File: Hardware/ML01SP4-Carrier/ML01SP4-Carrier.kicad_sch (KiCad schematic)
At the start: 3 parts, among them J1 NRF24L01P-ML01SP4, J2 Conn_01x05, J3 Conn_01x03

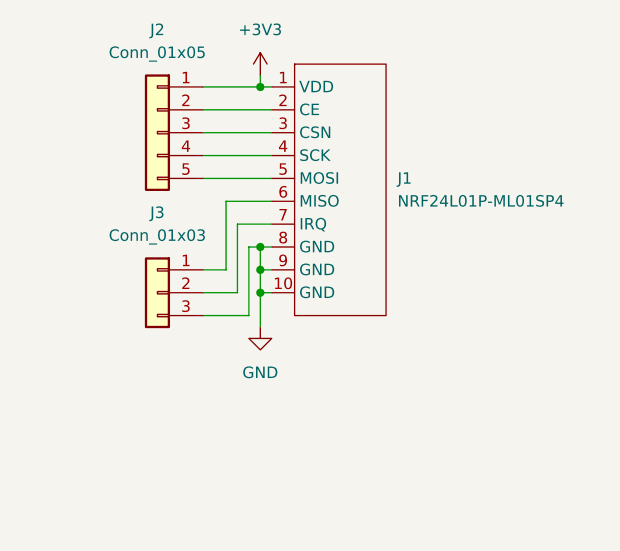
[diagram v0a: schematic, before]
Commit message: added decoupling capacitors and rounded pcb corners
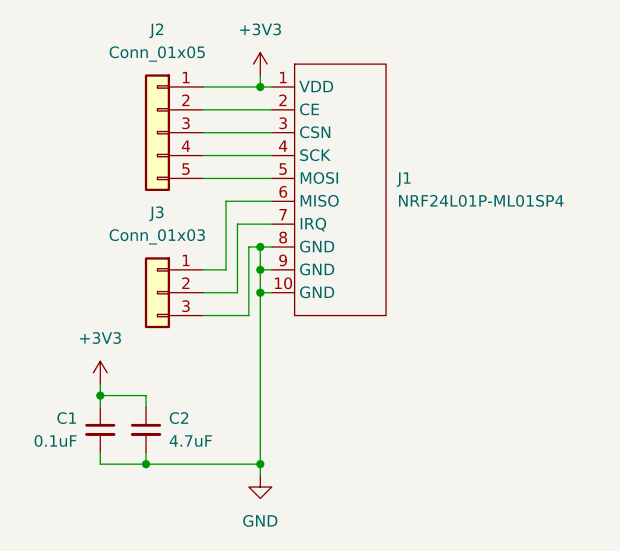
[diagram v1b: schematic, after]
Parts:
- added C1: 0.1uF, Capacitor_SMD:C_0603_1608Metric, symbol Device:C_Small
- added C2: 4.7uF, symbol Device:C_Small
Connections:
- net +3V3: now also C1.1, C2.1
- net GND: now also C1.2, C2.2
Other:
- title: (none) -> ML01SP4 Carrier
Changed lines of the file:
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@@
 (kicad_sch (version 20211123) (generator eeschema)
   (paper "A4")
+  (title_block
+    (title "ML01SP4 Carrier")
+    (date "2023-01-12")
+  )
   (junction (at 143.51 113.03) (diameter 0) (color 0 0 0 0)
   )
   (junction (at 143.51 107.95) (diameter 0) (color 0 0 0 0)
   )
+  (junction (at 143.51 132.08) (diameter 0) (color 0 0 0 0)
+  )
+  (junction (at 125.73 124.46) (diameter 0) (color 0 0 0 0)
+  )
+  (junction (at 130.81 132.08) (diameter 0) (color 0 0 0 0)
+  )
   (junction (at 143.51 110.49) (diameter 0) (color 0 0 0 0)
   )
@@
     (stroke (width 0) (type default) (color 0 0 0 0))
   )
+  (wire (pts (xy 143.51 113.03) (xy 143.51 132.08))
+    (stroke (width 0) (type default) (color 0 0 0 0))
+  )
   (wire (pts (xy 137.16 90.17) (xy 143.51 90.17))
     (stroke (width 0) (type default) (color 0 0 0 0))
   )
+  (wire (pts (xy 130.81 125.73) (xy 130.81 124.46))
+    (stroke (width 0) (type default) (color 0 0 0 0))
+  )
   (wire (pts (xy 139.7 110.49) (xy 137.16 110.49))
     (stroke (width 0) (type default) (color 0 0 0 0))
   )
-  (wire (pts (xy 143.51 113.03) (xy 143.51 116.84))
+  (wire (pts (xy 125.73 130.81) (xy 125.73 132.08))
     (stroke (width 0) (type default) (color 0 0 0 0))
   )
@@
     (stroke (width 0) (type default) (color 0 0 0 0))
   )
+  (wire (pts (xy 130.81 132.08) (xy 143.51 132.08))
+    (stroke (width 0) (type default) (color 0 0 0 0))
+  )
   (wire (pts (xy 137.16 92.71) (xy 144.78 92.71))
     (stroke (width 0) (type default) (color 0 0 0 0))
@@
     (stroke (width 0) (type default) (color 0 0 0 0))
   )
+  (wire (pts (xy 130.81 124.46) (xy 125.73 124.46))
+    (stroke (width 0) (type default) (color 0 0 0 0))
+  )
   (wire (pts (xy 140.97 113.03) (xy 137.16 113.03))
     (stroke (width 0) (type default) (color 0 0 0 0))
   )
+  (wire (pts (xy 125.73 132.08) (xy 130.81 132.08))
+    (stroke (width 0) (type default) (color 0 0 0 0))
+  )
   (wire (pts (xy 139.7 102.87) (xy 139.7 110.49))
     (stroke (width 0) (type default) (color 0 0 0 0))
@@
     (stroke (width 0) (type default) (color 0 0 0 0))
   )
+  (wire (pts (xy 130.81 130.81) (xy 130.81 132.08))
+    (stroke (width 0) (type default) (color 0 0 0 0))
+  )
+  (wire (pts (xy 125.73 124.46) (xy 125.73 125.73))
+    (stroke (width 0) (type default) (color 0 0 0 0))
+  )
+  (wire (pts (xy 143.51 132.08) (xy 143.51 133.35))
+    (stroke (width 0) (type default) (color 0 0 0 0))
+  )
   (wire (pts (xy 137.16 95.25) (xy 144.78 95.25))
+    (stroke (width 0) (type default) (color 0 0 0 0))
+  )
+  (wire (pts (xy 125.73 123.19) (xy 125.73 124.46))
     (stroke (width 0) (type default) (color 0 0 0 0))
   )
@@
     (pin "3")
   )
-  (symbol (lib_id "power:GND") (at 143.51 116.84 0) (unit 1)
-    (in_bom yes) (on_board yes) (fields_autoplaced)
-    (property "Reference" "#PWR0101" (id 0) (at 143.51 123.19 0)
-      (effects (font (size 1.27 1.27)) hide)
-    )
-    (property "Value" "GND" (id 1) (at 143.51 121.92 0))
-    (property "Footprint" "" (id 2) (at 143.51 116.84 0)
-      (effects (font (size 1.27 1.27)) hide)
-    )
-    (property "Datasheet" "" (id 3) (at 143.51 116.84 0)
+  (symbol (lib_id "Device:C_Small") (at 130.81 128.27 0) (unit 1)
+    (in_bom yes) (on_board yes) (fields_autoplaced)
+    (property "Reference" "C2" (id 0) (at 133.35 127.0062 0)
+      (effects (font (size 1.27 1.27)) (justify left))
+    )
+    (property "Value" "4.7uF" (id 1) (at 133.35 129.5462 0)
+      (effects (font (size 1.27 1.27)) (justify left))
+    )
+    (property "Footprint" "" (id 2) (at 130.81 128.27 0)
+      (effects (font (size 1.27 1.27)) hide)
+    )
+    (property "Datasheet" "~" (id 3) (at 130.81 128.27 0)
+      (effects (font (size 1.27 1.27)) hide)
+    )
+    (pin "1")
+    (pin "2")
+  )
+  (symbol (lib_id "power:GND") (at 143.51 133.35 0) (unit 1)
+    (in_bom yes) (on_board yes) (fields_autoplaced)
+    (property "Reference" "#PWR0101" (id 0) (at 143.51 139.7 0)
+      (effects (font (size 1.27 1.27)) hide)
+    )
+    (property "Value" "GND" (id 1) (at 143.51 138.43 0))
+    (property "Footprint" "" (id 2) (at 143.51 133.35 0)
+      (effects (font (size 1.27 1.27)) hide)
+    )
+    (property "Datasheet" "" (id 3) (at 143.51 133.35 0)
       (effects (font (size 1.27 1.27)) hide)
     )
@@
     (pin "5")
   )
+  (symbol (lib_id "power:+3V3") (at 125.73 123.19 0) (unit 1)
+    (in_bom yes) (on_board yes) (fields_autoplaced)
+    (property "Reference" "#PWR0103" (id 0) (at 125.73 127 0)
+      (effects (font (size 1.27 1.27)) hide)
+    )
+    (property "Value" "+3V3" (id 1) (at 125.73 118.11 0))
+    (property "Footprint" "" (id 2) (at 125.73 123.19 0)
+      (effects (font (size 1.27 1.27)) hide)
+    )
+    (property "Datasheet" "" (id 3) (at 125.73 123.19 0)
+      (effects (font (size 1.27 1.27)) hide)
+    )
+    (pin "1")
+  )
+  (symbol (lib_id "Device:C_Small") (at 125.73 128.27 0) (unit 1)
+    (in_bom yes) (on_board yes) (fields_autoplaced)
+    (property "Reference" "C1" (id 0) (at 123.19 127.0062 0)
+      (effects (font (size 1.27 1.27)) (justify right))
+    )
+    (property "Value" "0.1uF" (id 1) (at 123.19 129.5462 0)
+      (effects (font (size 1.27 1.27)) (justify right))
+    )
+    (property "Footprint" "Capacitor_SMD:C_0603_1608Metric" (id 2) (at 125.73 128.27 0)
+      (effects (font (size 1.27 1.27)) hide)
+    )
+    (property "Datasheet" "~" (id 3) (at 125.73 128.27 0)
+      (effects (font (size 1.27 1.27)) hide)
+    )
+    (pin "1")
+    (pin "2")
+  )
   (sheet_instances
     (path "/" (page "1"))
@@
       (reference "#PWR0102") (unit 1) (value "+3V3") (footprint "")
     )
+    (path "/f27d03a2-f7e2-4960-93cb-c1e734fd3d2d"
+      (reference "#PWR0103") (unit 1) (value "+3V3") (footprint "")
+    )
+    (path "/f3aace90-65a4-47de-94d8-e44c7248eac6"
+      (reference "C1") (unit 1) (value "0.1uF") (footprint "Capacitor_SMD:C_0603_1608Metric")
+    )
+    (path "/971ade52-ad43-4e5a-a04b-eeed39f9d363"
+      (reference "C2") (unit 1) (value "4.7uF") (footprint "Capacitor_SMD:C_0603_1608Metric")
+    )
     (path "/1eb9b296-a4da-47b3-b966-63173c3f3b73"
